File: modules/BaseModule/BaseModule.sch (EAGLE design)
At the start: 10 parts, among them J1 4P-2.0-90D

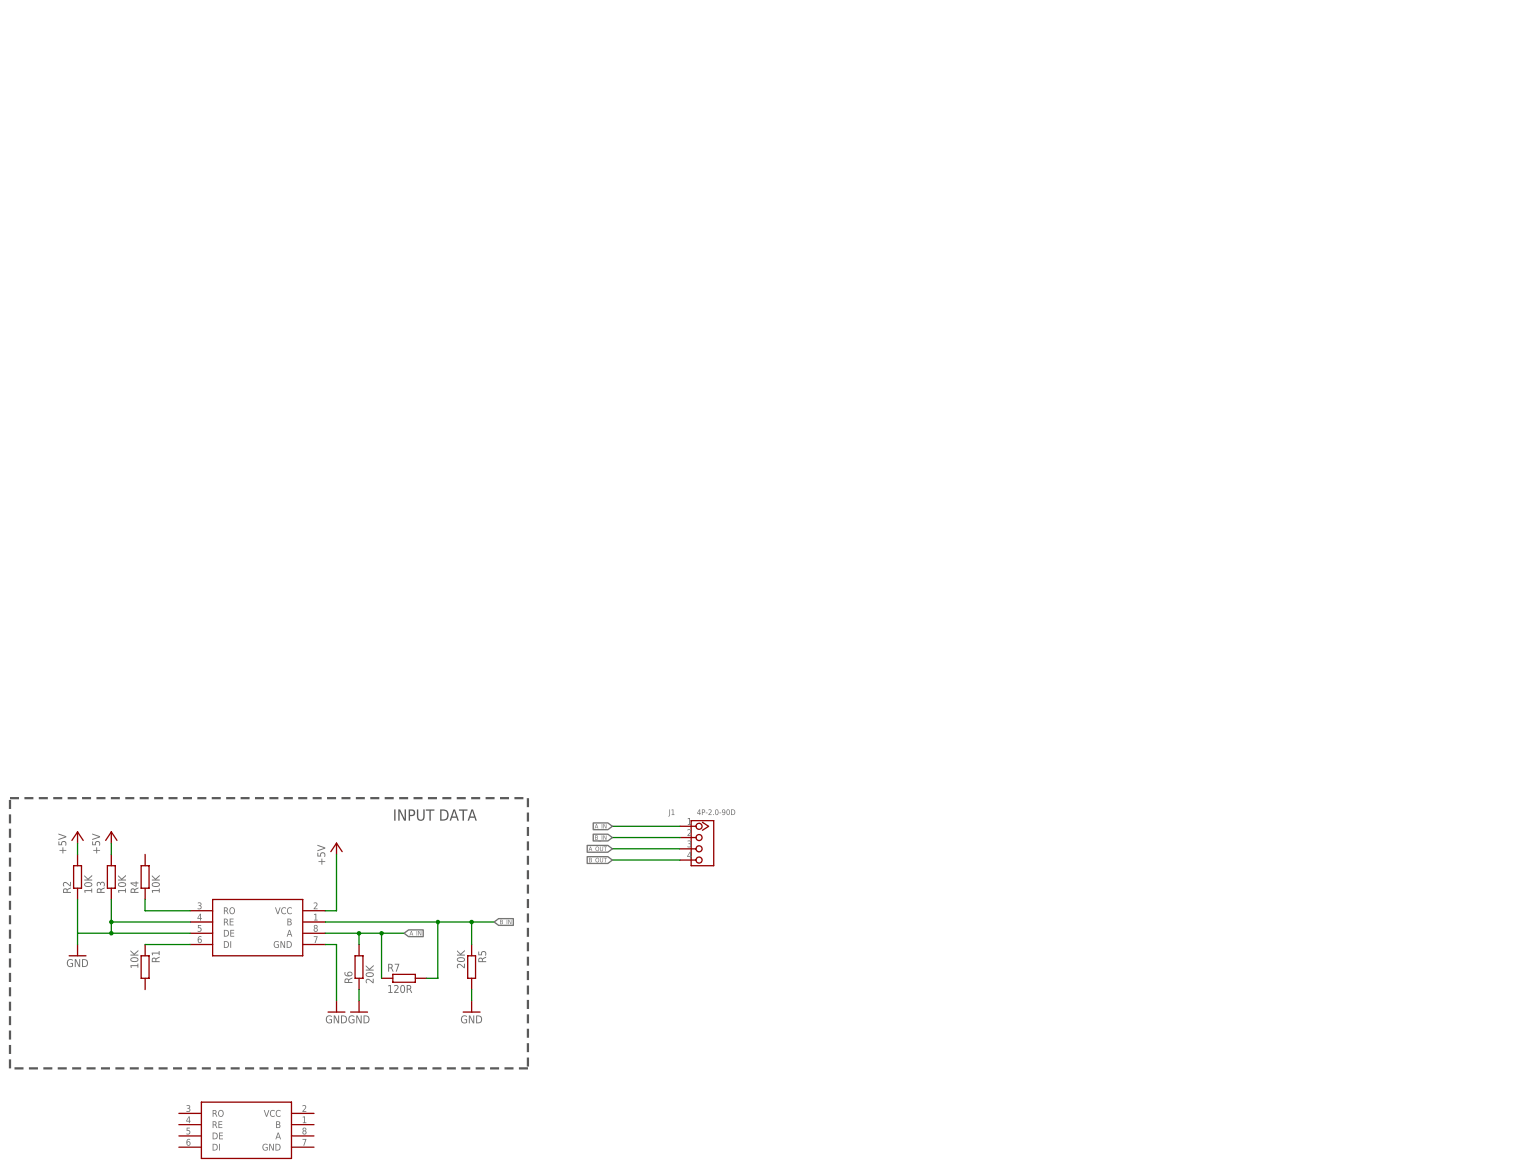
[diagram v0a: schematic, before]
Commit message: BaseBoard updates + hardware documentation
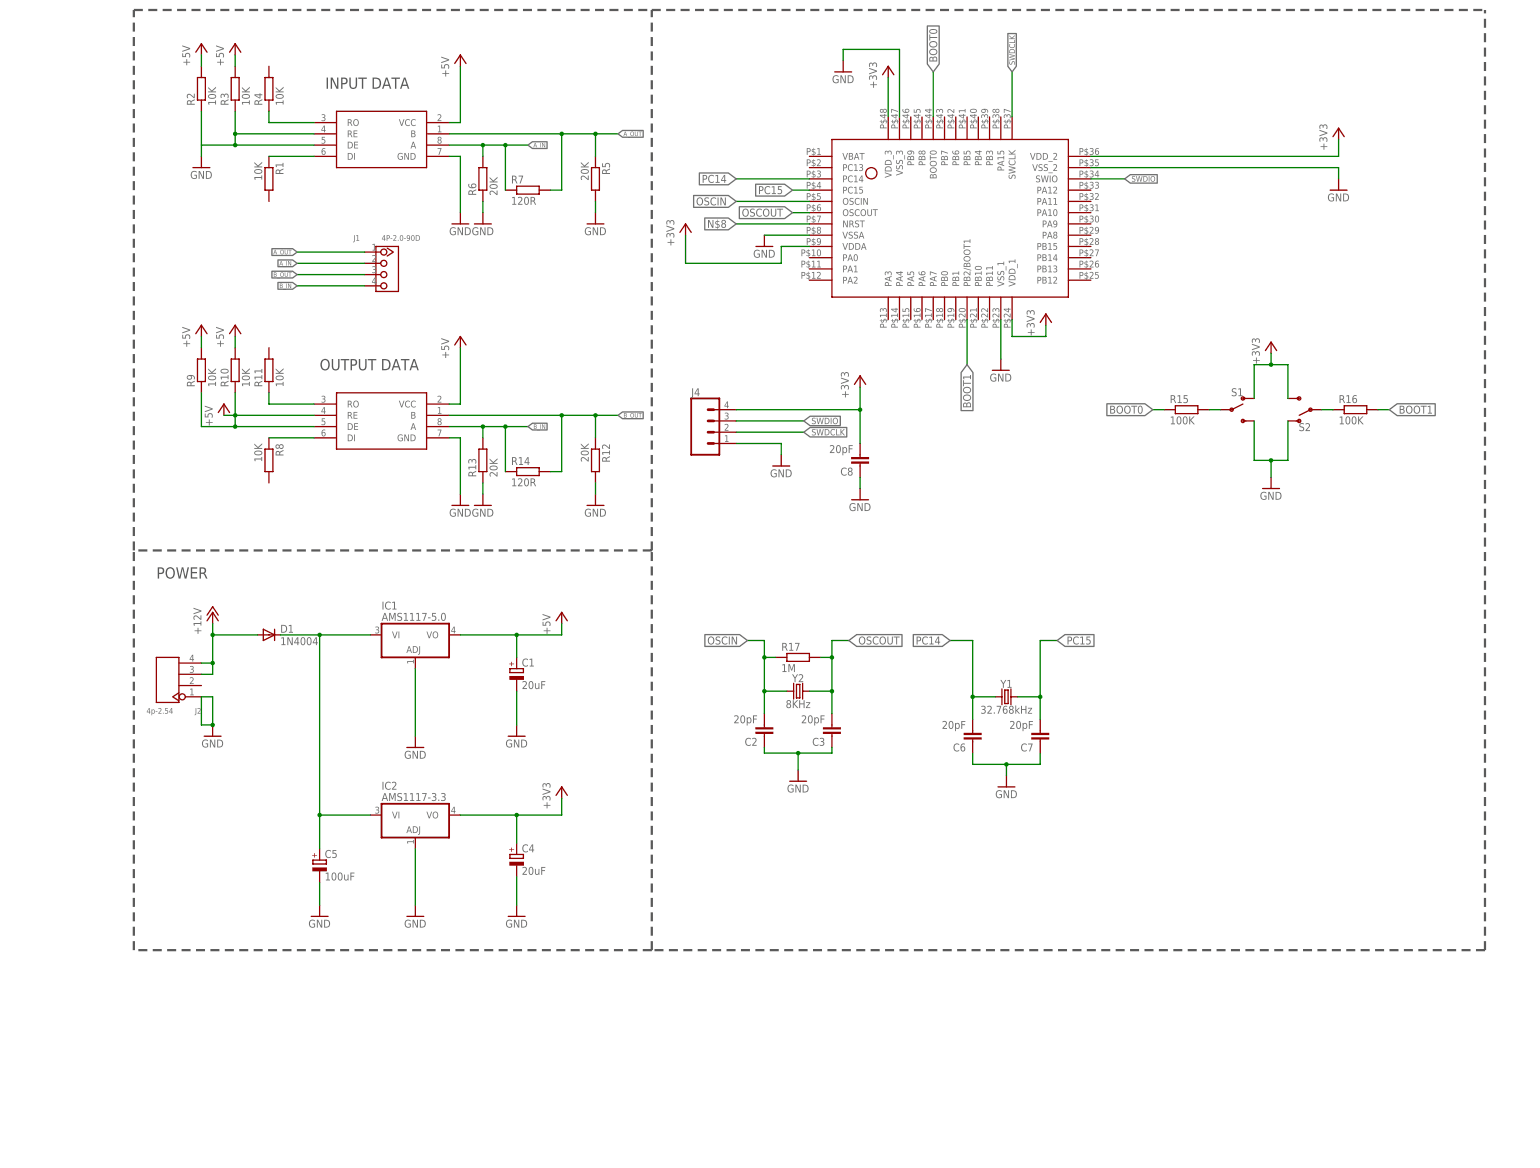
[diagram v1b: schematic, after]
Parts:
- added C1, C4: 20uF, rcl:CPOL-EU153CLV-0405
- added C2, C3, C6, C7, C8: 20pF, rcl:C-EUC0805
- added C5: 100uF, rcl:CPOL-EU153CLV-0405
- added D1: 1N4004, diode:1N4004
- added IC1: AMS1117-5.0, linear:317EMP
- added IC2: AMS1117-3.3, linear:317EMP
- added J2: 4p-2.54, Seeed-Connector:DIP-BLACK-MALE-HEADER-VERT(4P-2.54)
- added J4: (no value), SparkFun-Connectors:CONN_04
- added R10, R11, R8, R9: 10K, rcl:R-EU_R0603
- added R12, R13: 20K, rcl:R-EU_R0603
- added R14: 120R, rcl:R-EU_R0603
- added R15, R16: 100K, rcl:R-EU_R0805
- added R17: 1M, rcl:R-EU_R0805
- added S1, S2: (no value), SparkFun-Switches:SWITCH-SPDT-PTH-11.6X4.0MM-LOCK
- added U$3: STM32F103, Vaello:STM32F103
- added Y1: 32.768kHz, SparkFun-Clocks:CRYSTAL-32.768KHZSMD-MC146
- added Y2: 8KHz, SparkFun-Clocks:CRYSTALPTH-HC49US
- R1, R2, R3, R4, R5, R6, R7: device rcl:R-EU_R0805 -> rcl:R-EU_R0603
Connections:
- new net +12V: D1.A, J2.P$3, J2.P$4
- new net +3V3: C4.+, C8.2, IC2.VO, J4.4, S1.O, S2.S, U$3.VDDA, U$3.VDD_1, U$3.VDD_2, U$3.VDD_3
- new net BOOT0: R15.1, U$3.BOOT0
- new net BOOT1: R16.2, U$3.PB2/BOOT1
- new net N$2: R11.1, U$2.RO
- new net N$3: R8.1, U$2.DI
- new net N$5: R15.2, S1.P
- new net N$6: R16.1, S2.P
- new net N$8: U$3.NRST
- new net N$9: C5.+, D1.C, IC1.VI, IC2.VI
- new net OSCIN: C2.2, R17.1, U$3.OSCIN, Y2.1
- new net OSCOUT: C3.2, R17.2, U$3.OSCOUT, Y2.2
- new net PC14: C6.2, U$3.PC14, Y1.1
- new net PC15: C7.2, U$3.PC15, Y1.2
- new net SWDCLK: J4.2, U$3.SWCLK
- new net SWDIO: J4.3, U$3.SWIO
- net +5V: now also C1.+, IC1.VO, R10.1, R10.2, R9.1, R9.2, U$2.DE, U$2.RE, U$2.VCC
- net A_IN: now also J1.2; no longer J1.1
- net A_OUT: now also J1.1, R5.1, R7.2, U$1.B; no longer J1.3
- net B_IN: now also J1.4, R13.2, R14.1, U$2.A; no longer J1.2, R5.1, R7.2, U$1.B
- net B_OUT: now also J1.3, R12.1, R14.2, U$2.B; no longer J1.4
- net GND: now also C1.-, C2.1, C3.1, C4.-, C5.-, C6.1, C7.1, C8.1, IC1.ADJ, IC2.ADJ, J2.P$1, J4.1, R12.2, R13.1, S1.S, S2.O, U$2.GND, U$3.VSSA, U$3.VSS_1, U$3.VSS_2, U$3.VSS_3
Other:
- note added: "OUTPUT DATA"
- note added: "POWER"
- moved on the sheet: J1, R1, R2, R3, R4, R5, R6, R7

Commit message: base module update
base module update
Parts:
- added J10, J11, J12, J13, J14, J15, J16, J17, J18, J5, J6, J7, J8, J9: (no value), SparkFun-Connectors:CONN_08"
- added J19, J20: (no value), SparkFun-Connectors:CONN_02
- added J3: (no value), SparkFun-Connectors:CONN_14
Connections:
- new net RX1: J19.1, R4.2, R8.2, U$3.PA10
- new net RX2: J20.1, R11.2, U$3.PA3
- new net TX1: J19.2, R1.2, U$3.PA9
- new net TX2: J20.2, U$3.PA2
